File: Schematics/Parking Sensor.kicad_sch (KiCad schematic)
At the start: 7 parts, among them M1 U?, SW1 SW_Push, U1 VL53L1X_Board, U2 WS2812

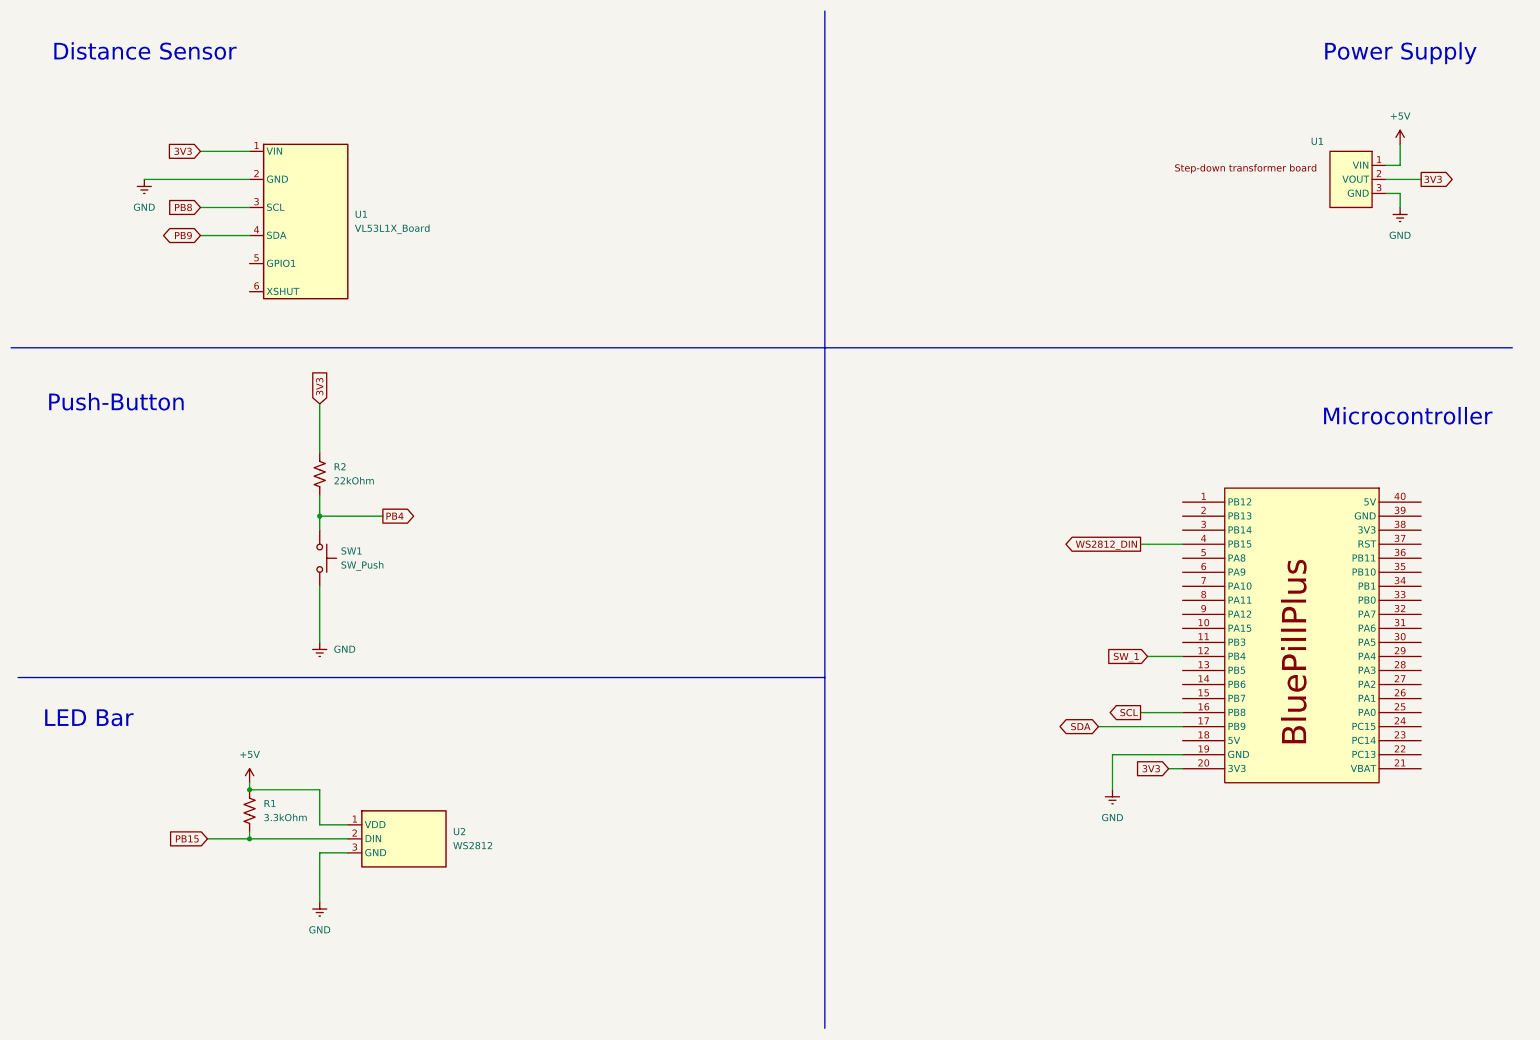
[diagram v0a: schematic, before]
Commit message: Updated schematics adding LIDAR interrupt and MOSFET to control LED bar power
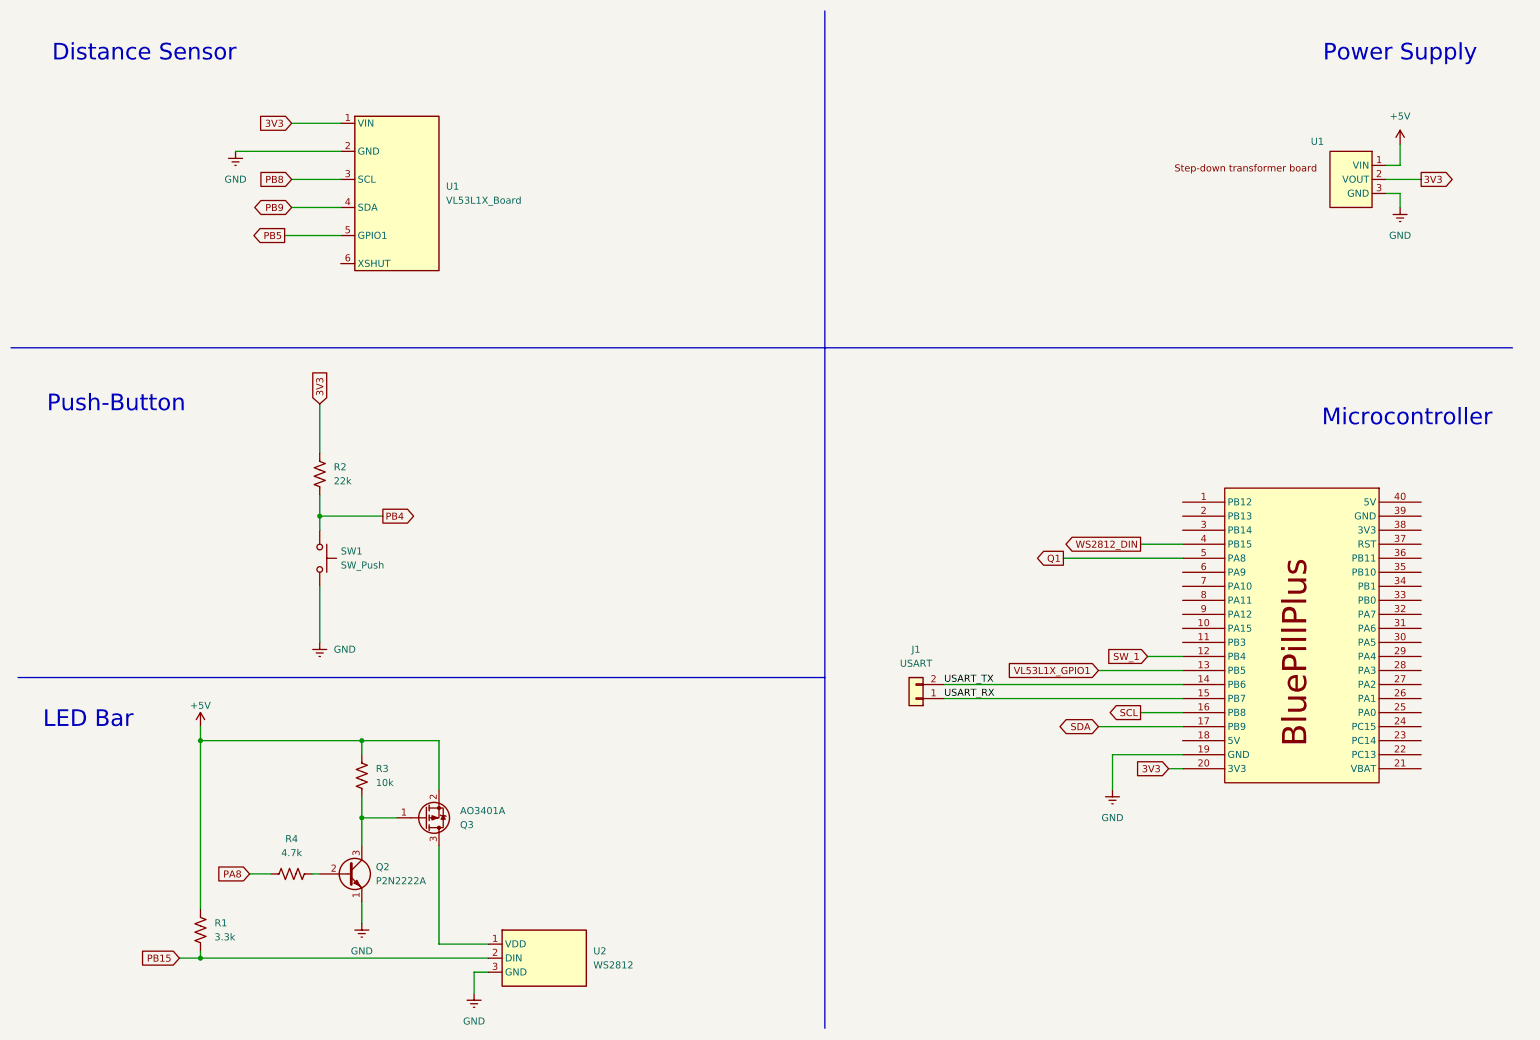
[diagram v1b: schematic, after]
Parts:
- added J1: USART, symbol Connector_Generic:Conn_01x02
- added Q2: P2N2222A, Package_TO_SOT_THT:TO-92_Inline, symbol Transistor_BJT:PN2222A
- added Q3: AO3401A, Package_TO_SOT_SMD:SOT-23, symbol Transistor_FET:AO3401A
- added R3: 10k, symbol Device:R_US
- added R4: 4.7k, symbol Device:R_US
- R1: value 3.3kOhm -> 3.3k
- R2: value 22kOhm -> 22k
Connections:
- net +5V: now also Q3.2 (S), R3.1; no longer U2.1 (VDD)
- net GND: now also Q2.1 (E)
- net PB5: now reaches U1.5 (GPIO1)
- net VL53L1X_GPIO1: now reaches M1.13 (PB5)
- net USART_TX: now reaches M1.14 (PB6)
- net USART_TX: now also J1.2 (Pin_2)
- net USART_RX: now reaches M1.15 (PB7)
- net USART_RX: now also J1.1 (Pin_1)
- net Q1: now reaches M1.5 (PA8)
- new net: Q2.2 (B), R4.2
- new net: Q3.3 (D), U2.1 (VDD)
- new net: Q2.3 (C), Q3.1 (G), R3.2
- new net PA8: R4.1
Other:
- moved on the sheet: R1, U1, U2
